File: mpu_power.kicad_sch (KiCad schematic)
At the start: 49 parts, among them U501 STM32MP135FAE7

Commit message: Reorganize schema
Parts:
- renumbered U501 to U401
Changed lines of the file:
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@@
 		)
 	)
-	(text_box "4.1. MPU power"
+	(text_box "4.2. MPU power"
 		(exclude_from_sim no)
 		(at 12.7 12.7 0)
@@
 		(on_board yes)
 		(dnp no)
-		(property "Reference" "U501"
+		(property "Reference" "U401"
 			(at 238.76 202.946 0)
 			(effects
@@
 			(project "linux-sbc"
 				(path "/fa11a02f-8043-4153-ab69-88d766503017/2d01087b-54dc-4f43-9cc7-a0ba17201776/38fb80ce-3aa2-4a17-bb8b-7759011755a2"
-					(reference "U501")
+					(reference "U401")
 					(unit 2)
 				)
@@
 		(on_board yes)
 		(dnp no)
-		(property "Reference" "U501"
+		(property "Reference" "U401"
 			(at 238.76 73.406 0)
 			(effects
@@
 			(project "linux-sbc"
 				(path "/fa11a02f-8043-4153-ab69-88d766503017/2d01087b-54dc-4f43-9cc7-a0ba17201776/38fb80ce-3aa2-4a17-bb8b-7759011755a2"
-					(reference "U501")
+					(reference "U401")
 					(unit 1)
 				)

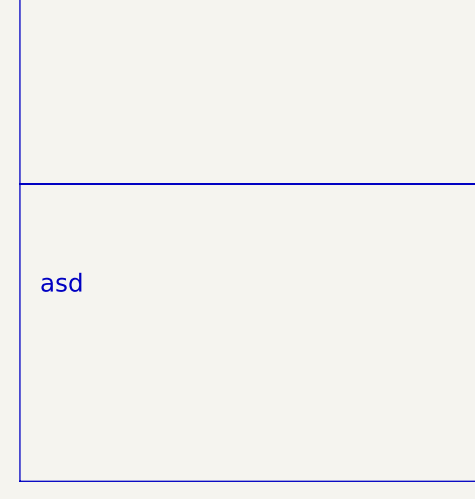
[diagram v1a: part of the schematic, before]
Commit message: Add MPU boot selection
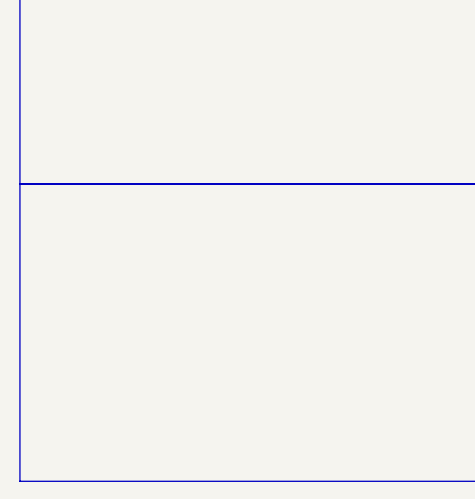
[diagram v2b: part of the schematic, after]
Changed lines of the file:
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@@
-		)
-	)
-	(text_box "asd"
-		(exclude_from_sim no)
-		(at 13.97 260.35 0)
-		(size 283.21 22.86)
-		(margins 0.9525 0.9525 0.9525 0.9525)
-		(stroke
-			(width -0.0001)
-			(type solid)
-		)
-		(fill
-			(type none)
-		)
-		(effects
-			(font
-				(size 2 2)
-			)
-			(justify left top)
 		)
 	)

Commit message: Refactor symbol properties
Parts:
- U401: Digi-Key Part Number_1 497-STM32MP135FAE7-ND -> (none); MPN_1 STM32MP135FAE7 -> (none); Manufacturer_1 STMicroelectronics -> (none)

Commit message: Refactor MPU and USB
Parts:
- U401: Digi-Key Part Number_1 (none) -> 497-STM32MP135FAE7-ND; MPN_1 (none) -> STM32MP135FAE7; Manufacturer_1 (none) -> STMicroelectronics
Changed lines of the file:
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@@
 			)
 		)
+		(property "Digi-Key Part Number_1" "497-STM32MP135FAE7-ND"
+			(at 238.76 110.49 0)
+			(effects
+				(font
+					(size 1.27 1.27)
+				)
+				(hide yes)
+			)
+		)
+		(property "Manufacturer_1" "STMicroelectronics"
+			(at 238.76 110.49 0)
+			(effects
+				(font
+					(size 1.27 1.27)
+				)
+				(hide yes)
+			)
+		)
+		(property "MPN_1" "STM32MP135FAE7"
+			(at 238.76 110.49 0)
+			(effects
+				(font
+					(size 1.27 1.27)
+				)
+				(hide yes)
+			)
+		)
 		(pin "J6"
 		)
@@
 			(effects
 				(font
+					(size 1.27 1.27)
+				)
+				(hide yes)
+			)
+		)
+		(property "Digi-Key Part Number_1" "497-STM32MP135FAE7-ND"
+			(at 238.76 30.48 0)
+			(effects
+				(font
+					(size 1.27 1.27)
+				)
+				(hide yes)
+			)
+		)
+		(property "Manufacturer_1" "STMicroelectronics"
+			(at 238.76 30.48 0)
+			(effects
+				(font
+					(size 1.27 1.27)
+				)
+				(hide yes)
+			)
+		)
+		(property "MPN_1" "STM32MP135FAE7"
+			(at 238.76 30.48 0)
+			(effects
+				(font

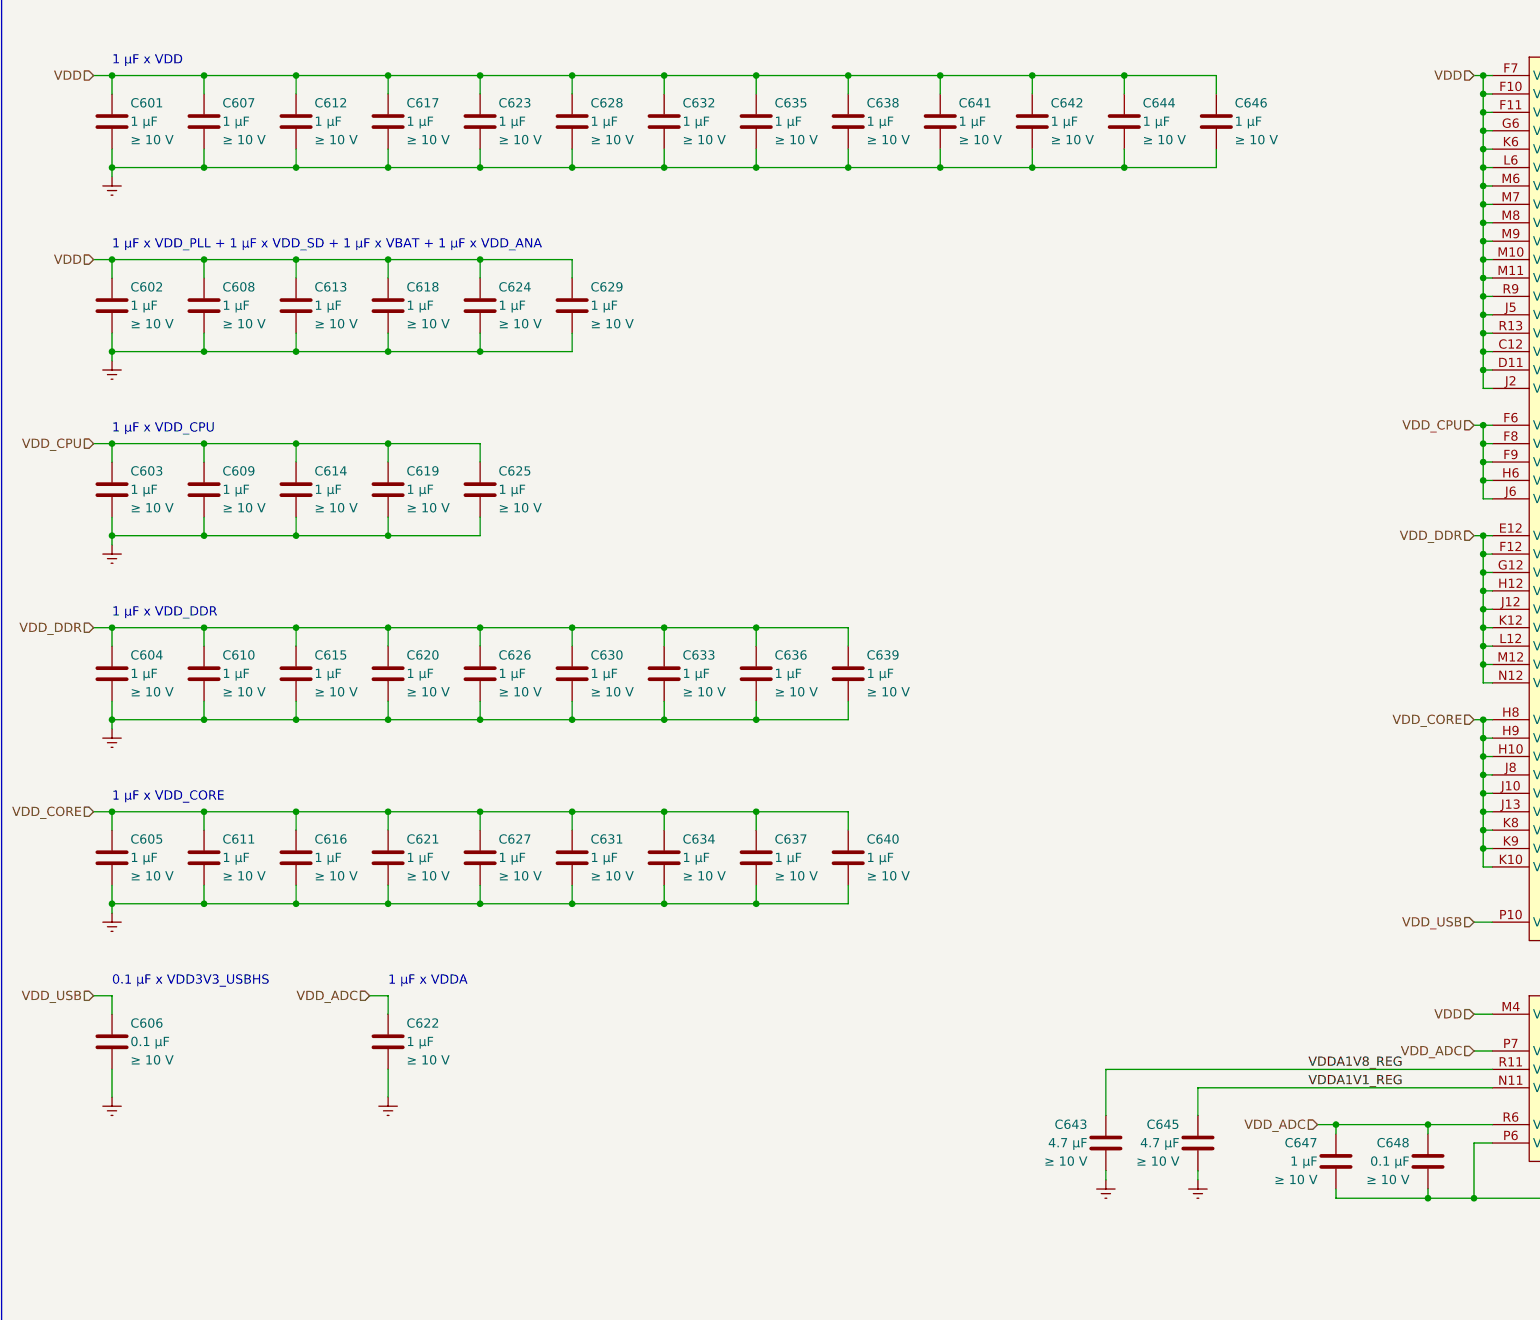
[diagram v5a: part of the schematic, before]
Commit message: Fix component values
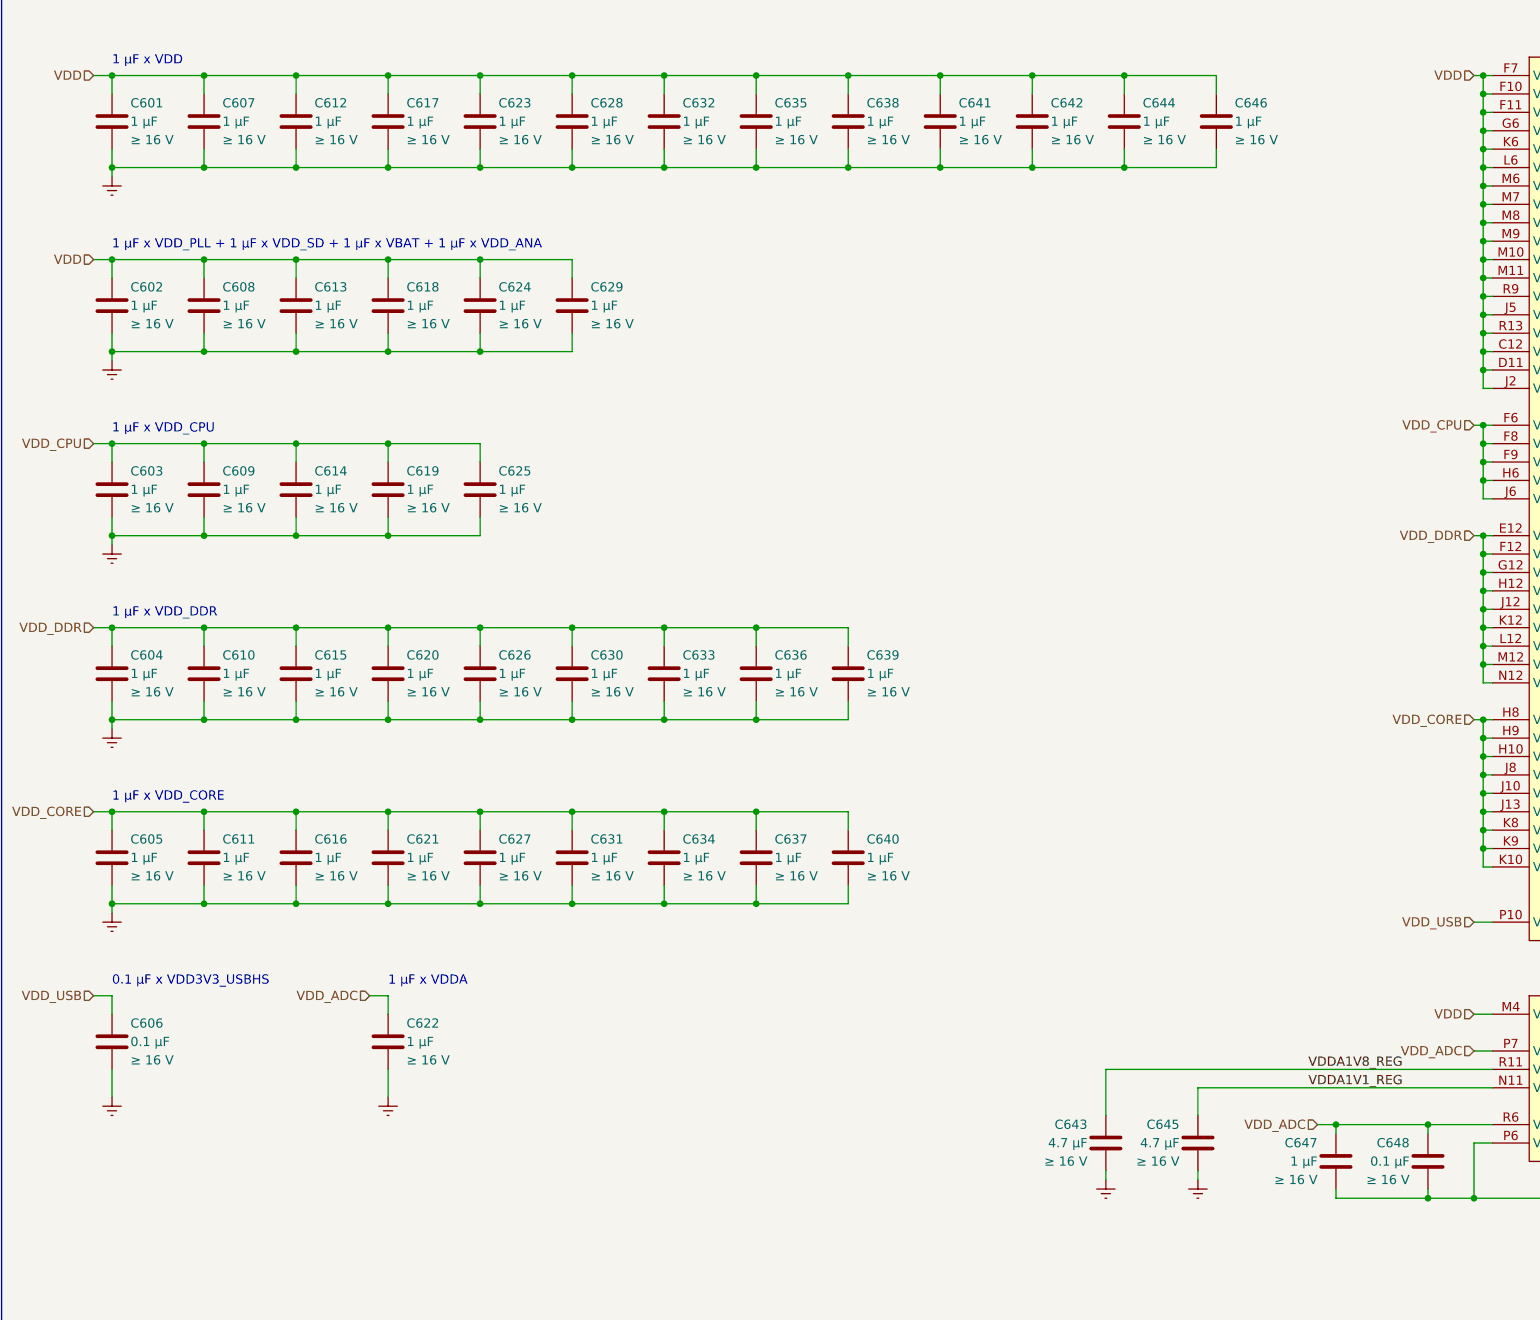
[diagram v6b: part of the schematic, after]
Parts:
- C601, C602, C603, C604, C605, C606, C607, C608, C609, C610, C611, C612, C613, C614, C615, C616, C617, C618, C619, C620, C621, C622, C623, C624, C625, C626, C627, C628, C629, C630, C631, C632, C633, C634, C635, C636, C637, C638, C639, C640, C641, C642, C643, C644, C645, C646, C647, C648: Voltage rating ≥ 10 V -> ≥ 16 V

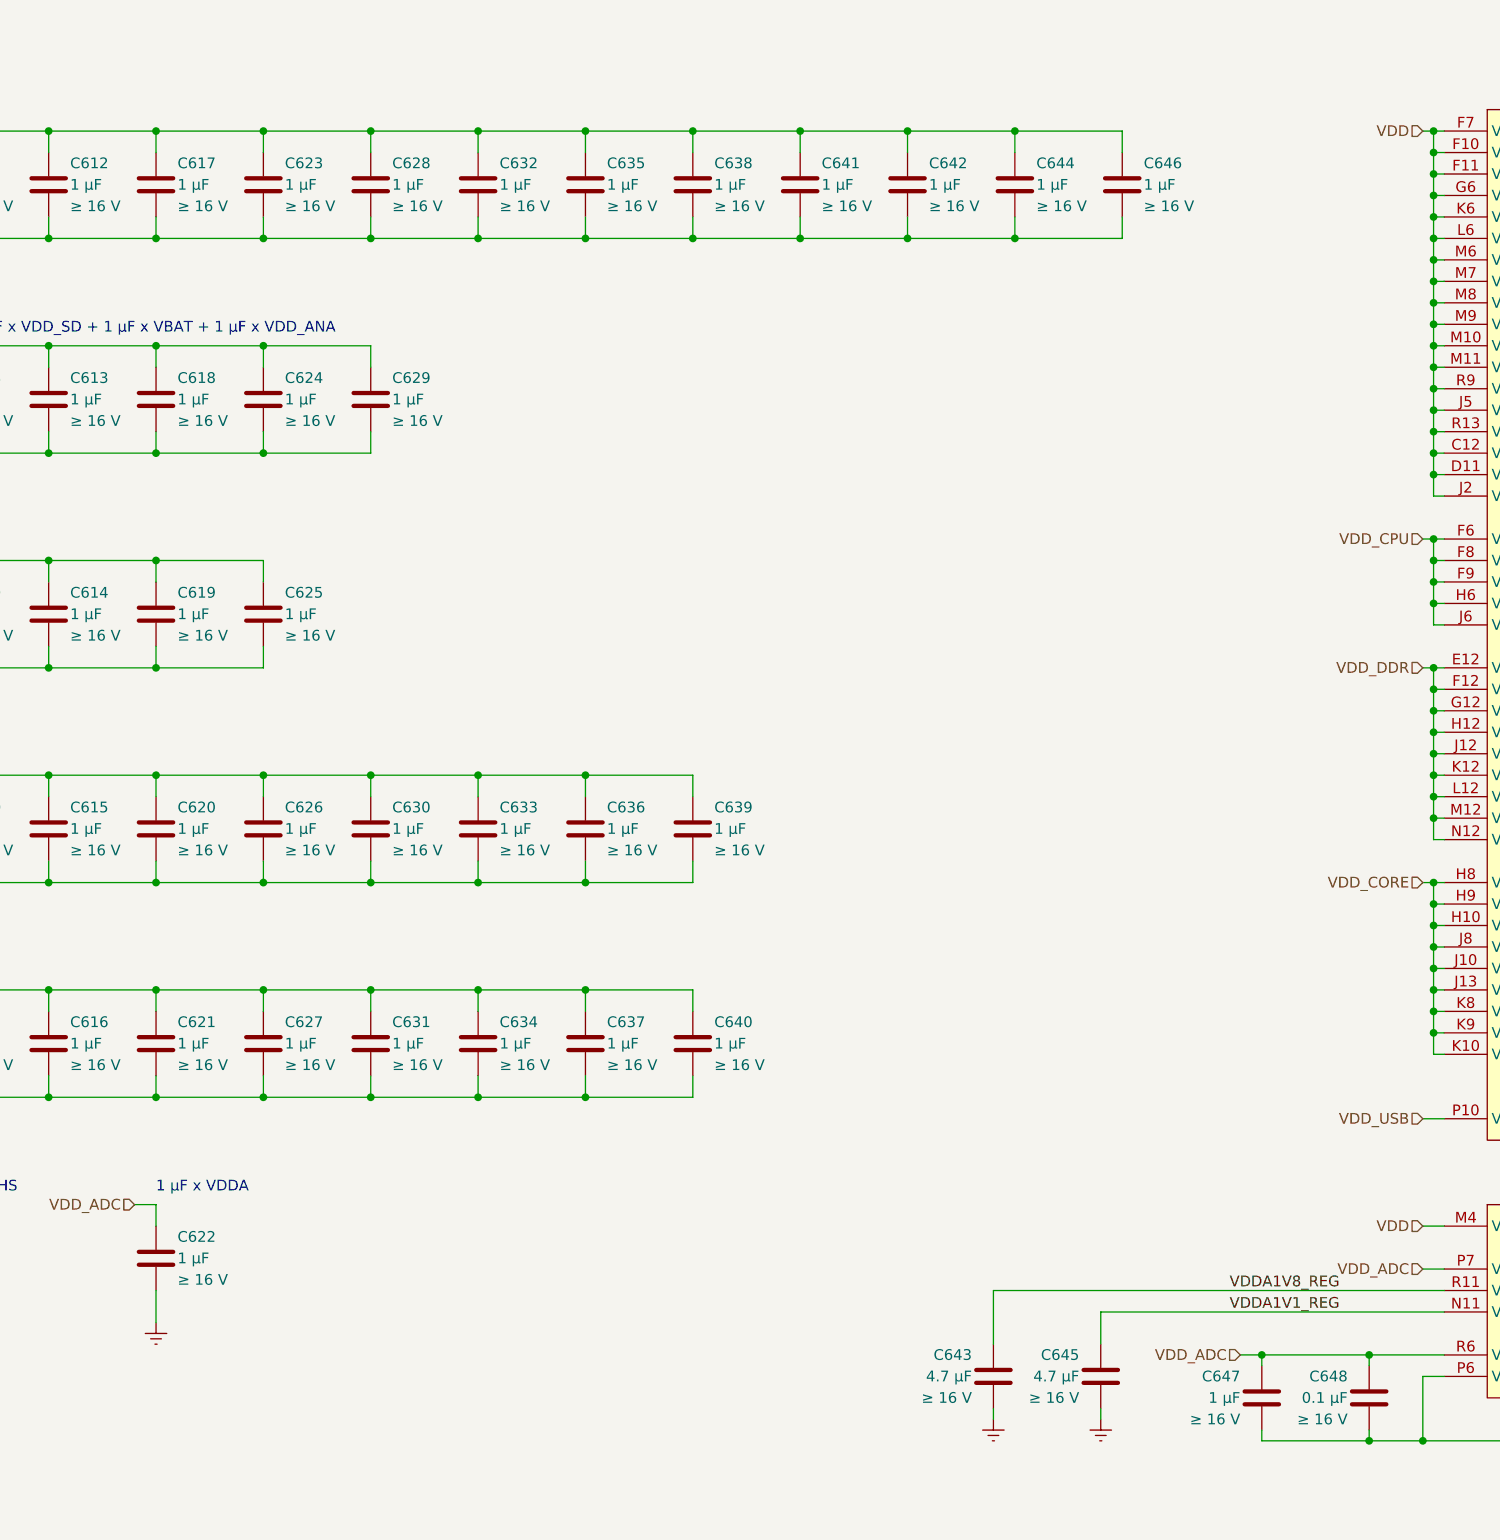
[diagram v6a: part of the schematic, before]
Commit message: Refactor schematics
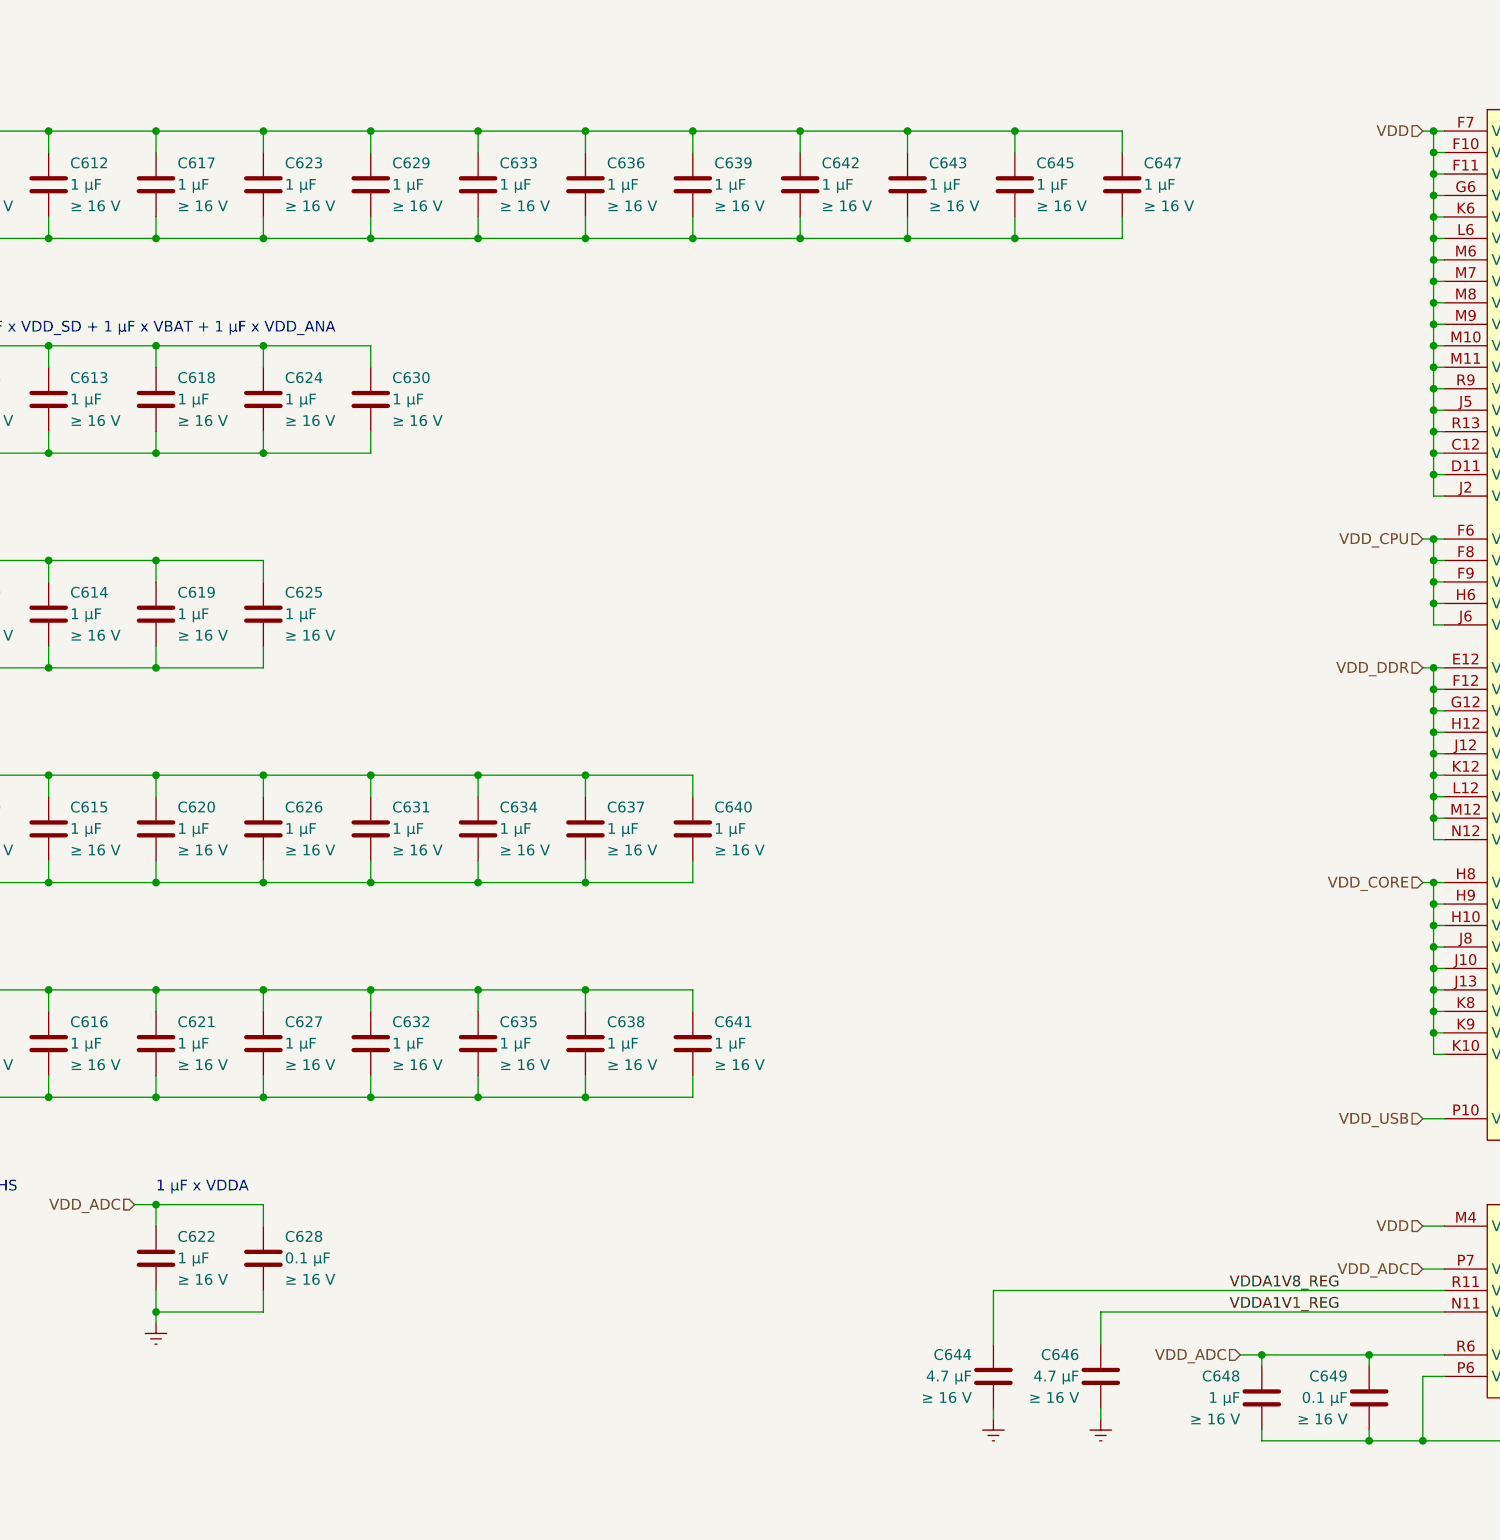
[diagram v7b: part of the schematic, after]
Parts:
- added C628: 0.1 µF, symbol Device:C
- renumbered C628 to C629, C629 to C630, C630 to C631, C631 to C632, C632 to C633, C633 to C634, C634 to C635, C635 to C636, C636 to C637, C637 to C638, C638 to C639, C639 to C640, C640 to C641, C641 to C642, C642 to C643, C643 to C644, C644 to C645, C645 to C646, C646 to C647, C647 to C648, C648 to C649
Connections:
- net GND: now also C628.2
- net VDD_ADC: now also C628.1
